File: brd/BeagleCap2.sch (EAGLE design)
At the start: 33 parts, among them IC2 7805TV, J2 DS18B20, J3 Battery, U1 DHT22, X1 Conn BNC : pH, X2 Conn BNC : Dissolved Oxygen, X3 Conn BNC : Conductivity, X4 Conn BNC : ORP

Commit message: Schematic updated with new PCB
Done by JayMcGee
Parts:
- LED1: device led:LED5MM -> led:LEDSML0805
- R1, R10, R2, R3, R4, R5, R6, R7, R8, R9: device adafruit:R-US_0207/10 -> adafruit:R-US_R0805
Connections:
- removed net 3.3V: J2.3, J4.1, R10.1, R2.2, R4.1, R5.2, R6.2, R9.1, U$1.VDD_3V3EXP@2, U$2.VCC, U$3.VCC, U$4.VCC, U$5.VCC, U1.VDD
- new net GNDX: J2.3, R2.2, R4.1, R5.2, R6.2, U$1.VDD_3V3EXP@2, U$2.VCC, U$3.VCC, U$4.VCC, U$5.VCC, U1.VDD
- net 5V: now also J4.1, R10.1, R9.1
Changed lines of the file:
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@@
 <part name="SUPPLY3" library="supply2" deviceset="GND" device=""/>
 <part name="P+2" library="supply1" deviceset="VCC" device="" value="3.3V"/>
-<part name="R1" library="adafruit" deviceset="R-US_" device="0207/10" value="100"/>
-<part name="R2" library="adafruit" deviceset="R-US_" device="0207/10" value="4.7K"/>
-<part name="R3" library="adafruit" deviceset="R-US_" device="0207/10" value="100"/>
-<part name="R4" library="adafruit" deviceset="R-US_" device="0207/10" value="4.7K"/>
+<part name="R1" library="adafruit" deviceset="R-US_" device="R0805" value="100"/>
+<part name="R2" library="adafruit" deviceset="R-US_" device="R0805" value="4.7K"/>
+<part name="R3" library="adafruit" deviceset="R-US_" device="R0805" value="100"/>
+<part name="R4" library="adafruit" deviceset="R-US_" device="R0805" value="4.7K"/>
 <part name="3.3V" library="supply1" deviceset="VCC" device="" value="3.3V"/>
 <part name="IC2" library="linear" deviceset="78*" device="TV" technology="05"/>
@@
 <part name="SUPPLY5" library="supply2" deviceset="GND" device=""/>
 <part name="P+5" library="supply1" deviceset="VCC" device="" value="3.3V"/>
-<part name="R5" library="adafruit" deviceset="R-US_" device="0207/10" value="4.7K"/>
-<part name="R6" library="adafruit" deviceset="R-US_" device="0207/10" value="4.7K"/>
+<part name="R5" library="adafruit" deviceset="R-US_" device="R0805" value="4.7K"/>
+<part name="R6" library="adafruit" deviceset="R-US_" device="R0805" value="4.7K"/>
 <part name="SUPPLY6" library="supply2" deviceset="GND" device=""/>
 <part name="BARREL" library="con-wago-500" deviceset="W237-102" device=""/>
 <part name="D1" library="diode" deviceset="1N4004" device="" value="1N4007"/>
 <part name="D2" library="diode" deviceset="1N4004" device="" value="1N4007"/>
-<part name="LED1" library="led" deviceset="LED" device="5MM"/>
-<part name="R7" library="adafruit" deviceset="R-US_" device="0207/10" value="330"/>
-<part name="R8" library="adafruit" deviceset="R-US_" device="0207/10" value="1K"/>
+<part name="LED1" library="led" deviceset="LED" device="SML0805"/>
+<part name="R7" library="adafruit" deviceset="R-US_" device="R0805" value="330"/>
+<part name="R8" library="adafruit" deviceset="R-US_" device="R0805" value="1K"/>
 <part name="D3" library="diode" deviceset="1N4148" device="DO35-10"/>
-<part name="R9" library="adafruit" deviceset="R-US_" device="0207/10" value="4.7K"/>
+<part name="R9" library="adafruit" deviceset="R-US_" device="R0805" value="4.7K"/>
 <part name="D4" library="diode" deviceset="1N4148" device="DO35-10"/>
-<part name="R10" library="adafruit" deviceset="R-US_" device="0207/10" value="4.7K"/>
-<part name="SUPPLY7" library="supply2" deviceset="VCC" device=""/>
+<part name="R10" library="adafruit" deviceset="R-US_" device="R0805" value="4.7K"/>
 <part name="J2" library="con-amp" deviceset="MTA03-100" device="" value="DS18B20"/>
 <part name="J3" library="con-amp" deviceset="MTA03-100" device="" value="Battery"/>
@@
 <instance part="D4" gate="G$1" x="83.82" y="-49.53"/>
 <instance part="R10" gate="G$1" x="101.6" y="-34.29" rot="R270"/>
-<instance part="SUPPLY7" gate="G$1" x="88.9" y="-24.13"/>
 <instance part="J2" gate="G$1" x="-66.04" y="104.14" rot="R90"/>
 <instance part="J3" gate="G$1" x="-8.89" y="154.94" rot="R90"/>
@@
 </segment>
 </net>
-<net name="3.3V" class="0">
+<net name="GNDX" class="0">
 <segment>
 <wire x1="76.2" y1="45.72" x2="76.2" y2="48.26" width="0.1524" layer="91"/>
@@
 <pinref part="R6" gate="G$1" pin="2"/>
 <wire x1="92.71" y1="41.91" x2="92.71" y2="39.37" width="0.1524" layer="91"/>
-</segment>
-<segment>
-<pinref part="SUPPLY7" gate="G$1" pin="VCC"/>
-<wire x1="88.9" y1="-26.67" x2="88.9" y2="-27.94" width="0.1524" layer="91"/>
-<pinref part="R9" gate="G$1" pin="1"/>
-<wire x1="92.71" y1="-29.21" x2="92.71" y2="-27.94" width="0.1524" layer="91"/>
-<wire x1="92.71" y1="-27.94" x2="88.9" y2="-27.94" width="0.1524" layer="91"/>
-<pinref part="R10" gate="G$1" pin="1"/>
-<wire x1="101.6" y1="-29.21" x2="101.6" y2="-27.94" width="0.1524" layer="91"/>
-<wire x1="101.6" y1="-27.94" x2="92.71" y2="-27.94" width="0.1524" layer="91"/>
-<junction x="92.71" y="-27.94"/>
-<wire x1="101.6" y1="-27.94" x2="106.68" y2="-27.94" width="0.1524" layer="91"/>
-<junction x="101.6" y="-27.94"/>
-<wire x1="106.68" y1="-27.94" x2="106.68" y2="-40.64" width="0.1524" layer="91"/>
-<pinref part="J4" gate="G$1" pin="1"/>
-<wire x1="106.68" y1="-40.64" x2="125.73" y2="-40.64" width="0.1524" layer="91"/>
 </segment>
 </net>
@@
 <wire x1="66.04" y1="156.21" x2="66.04" y2="157.48" width="0.1524" layer="91"/>
 <junction x="66.04" y="157.48"/>
-</segment>
-</net>
+<label x="66.04" y="158.75" size="1.778" layer="95"/>
+</segment>
+<segment>
+<pinref part="R9" gate="G$1" pin="1"/>
+<wire x1="92.71" y1="-29.21" x2="92.71" y2="-27.94" width="0.1524" layer="91"/>
+<wire x1="92.71" y1="-27.94" x2="101.6" y2="-27.94" width="0.1524" layer="91"/>
+<pinref part="R10" gate="G$1" pin="1"/>
+<wire x1="101.6" y1="-27.94" x2="101.6" y2="-29.21" width="0.1524" layer="91"/>
+<wire x1="101.6" y1="-27.94" x2="106.68" y2="-27.94" width="0.1524" layer="91"/>
+<junction x="101.6" y="-27.94"/>
+<wire x1="106.68" y1="-27.94" x2="106.68" y2="-40.64" width="0.1524" layer="91"/>
+<pinref part="J4" gate="G$1" pin="1"/>
+<wire x1="106.68" y1="-40.64" x2="125.73" y2="-40.64" width="0.1524" layer="91"/>
+<label x="92.71" y="-27.94" size="1.778" layer="95"/>
+<wire x1="92.71" y1="-27.94" x2="90.17" y2="-27.94" width="0.1524" layer="91"/>
+<junction x="92.71" y="-27.94"/>
+<wire x1="90.17" y1="-27.94" x2="90.17" y2="-24.13" width="0.1524" layer="91"/>
+</segment>
+</net>

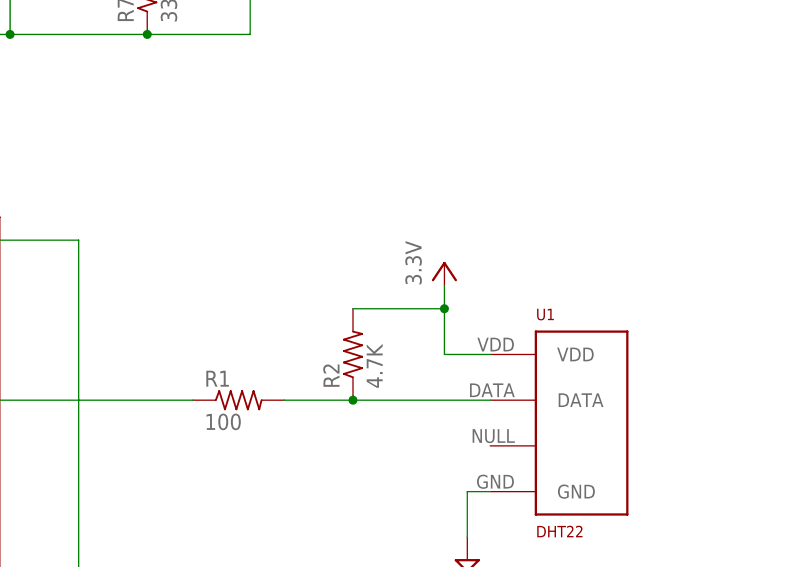
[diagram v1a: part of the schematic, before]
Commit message: Pcb updated, Fixed DRU error
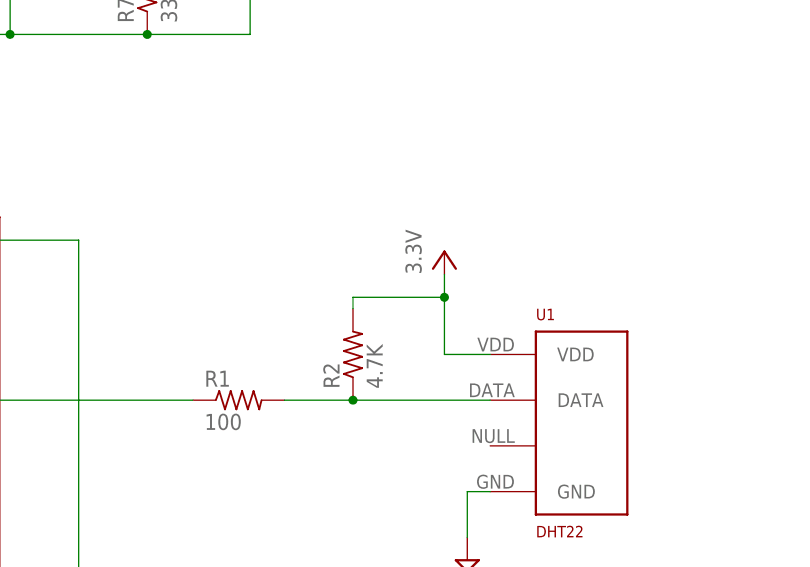
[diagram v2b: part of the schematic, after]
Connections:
- net GNDX renamed 3.3V
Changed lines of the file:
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@@
 <grid distance="0.05" unitdist="inch" unit="inch" style="lines" multiple="1" display="no" altdistance="0.01" altunitdist="inch" altunit="inch"/>
 <layers>
-<layer number="1" name="Top" color="4" fill="1" visible="yes" active="no"/>
-<layer number="2" name="Route2" color="1" fill="3" visible="yes" active="no"/>
-<layer number="3" name="Route3" color="4" fill="3" visible="yes" active="no"/>
-<layer number="4" name="Route4" color="1" fill="4" visible="yes" active="no"/>
-<layer number="5" name="Route5" color="4" fill="4" visible="yes" active="no"/>
-<layer number="6" name="Route6" color="1" fill="8" visible="yes" active="no"/>
-<layer number="7" name="Route7" color="4" fill="8" visible="yes" active="no"/>
-<layer number="8" name="Route8" color="1" fill="2" visible="yes" active="no"/>
-<layer number="9" name="Route9" color="4" fill="2" visible="yes" active="no"/>
-<layer number="10" name="Route10" color="1" fill="7" visible="yes" active="no"/>
-<layer number="11" name="Route11" color="4" fill="7" visible="yes" active="no"/>
-<layer number="12" name="Route12" color="1" fill="5" visible="yes" active="no"/>
-<layer number="13" name="Route13" color="4" fill="5" visible="yes" active="no"/>
-<layer number="14" name="Route14" color="1" fill="6" visible="yes" active="no"/>
-<layer number="15" name="Route15" color="4" fill="6" visible="yes" active="no"/>
-<layer number="16" name="Bottom" color="1" fill="1" visible="yes" active="no"/>
-<layer number="17" name="Pads" color="2" fill="1" visible="yes" active="no"/>
-<layer number="18" name="Vias" color="2" fill="1" visible="yes" active="no"/>
-<layer number="19" name="Unrouted" color="6" fill="1" visible="yes" active="no"/>
-<layer number="20" name="Dimension" color="15" fill="1" visible="yes" active="no"/>
-<layer number="21" name="tPlace" color="7" fill="1" visible="yes" active="no"/>
-<layer number="22" name="bPlace" color="7" fill="1" visible="yes" active="no"/>
-<layer number="23" name="tOrigins" color="15" fill="1" visible="yes" active="no"/>
-<layer number="24" name="bOrigins" color="15" fill="1" visible="yes" active="no"/>
-<layer number="25" name="tNames" color="7" fill="1" visible="yes" active="no"/>
-<layer number="26" name="bNames" color="7" fill="1" visible="yes" active="no"/>
-<layer number="27" name="tValues" color="7" fill="1" visible="yes" active="no"/>
-<layer number="28" name="bValues" color="7" fill="1" visible="yes" active="no"/>
+<layer number="1" name="Top" color="4" fill="1" visible="no" active="no"/>
+<layer number="2" name="Route2" color="1" fill="3" visible="no" active="no"/>
+<layer number="3" name="Route3" color="4" fill="3" visible="no" active="no"/>
+<layer number="4" name="Route4" color="1" fill="4" visible="no" active="no"/>
+<layer number="5" name="Route5" color="4" fill="4" visible="no" active="no"/>
+<layer number="6" name="Route6" color="1" fill="8" visible="no" active="no"/>
+<layer number="7" name="Route7" color="4" fill="8" visible="no" active="no"/>
+<layer number="8" name="Route8" color="1" fill="2" visible="no" active="no"/>
+<layer number="9" name="Route9" color="4" fill="2" visible="no" active="no"/>
+<layer number="10" name="Route10" color="1" fill="7" visible="no" active="no"/>
+<layer number="11" name="Route11" color="4" fill="7" visible="no" active="no"/>
+<layer number="12" name="Route12" color="1" fill="5" visible="no" active="no"/>
+<layer number="13" name="Route13" color="4" fill="5" visible="no" active="no"/>
+<layer number="14" name="Route14" color="1" fill="6" visible="no" active="no"/>
+<layer number="15" name="Route15" color="4" fill="6" visible="no" active="no"/>
+<layer number="16" name="Bottom" color="1" fill="1" visible="no" active="no"/>
+<layer number="17" name="Pads" color="2" fill="1" visible="no" active="no"/>
+<layer number="18" name="Vias" color="2" fill="1" visible="no" active="no"/>
+<layer number="19" name="Unrouted" color="6" fill="1" visible="no" active="no"/>
+<layer number="20" name="Dimension" color="15" fill="1" visible="no" active="no"/>
+<layer number="21" name="tPlace" color="7" fill="1" visible="no" active="no"/>
+<layer number="22" name="bPlace" color="7" fill="1" visible="no" active="no"/>
+<layer number="23" name="tOrigins" color="15" fill="1" visible="no" active="no"/>
+<layer number="24" name="bOrigins" color="15" fill="1" visible="no" active="no"/>
+<layer number="25" name="tNames" color="7" fill="1" visible="no" active="no"/>
+<layer number="26" name="bNames" color="7" fill="1" visible="no" active="no"/>
+<layer number="27" name="tValues" color="7" fill="1" visible="no" active="no"/>
+<layer number="28" name="bValues" color="7" fill="1" visible="no" active="no"/>
 <layer number="29" name="tStop" color="7" fill="3" visible="no" active="no"/>
 <layer number="30" name="bStop" color="7" fill="6" visible="no" active="no"/>
@@
 <layer number="35" name="tGlue" color="7" fill="4" visible="no" active="no"/>
 <layer number="36" name="bGlue" color="7" fill="5" visible="no" active="no"/>
-<layer number="37" name="tTest" color="7" fill="1" visible="yes" active="no"/>
-<layer number="38" name="bTest" color="7" fill="1" visible="yes" active="no"/>
+<layer number="37" name="tTest" color="7" fill="1" visible="no" active="no"/>
+<layer number="38" name="bTest" color="7" fill="1" visible="no" active="no"/>
 <layer number="39" name="tKeepout" color="4" fill="11" visible="no" active="no"/>
 <layer number="40" name="bKeepout" color="1" fill="11" visible="no" active="no"/>
@@
 <layer number="44" name="Drills" color="7" fill="1" visible="no" active="no"/>
 <layer number="45" name="Holes" color="7" fill="1" visible="no" active="no"/>
-<layer number="46" name="Milling" color="3" fill="1" visible="yes" active="no"/>
-<layer number="47" name="Measures" color="7" fill="1" visible="yes" active="no"/>
-<layer number="48" name="Document" color="7" fill="1" visible="yes" active="no"/>
-<layer number="49" name="Reference" color="7" fill="1" visible="yes" active="no"/>
-<layer number="50" name="dxf" color="7" fill="1" visible="yes" active="no"/>
-<layer number="51" name="tDocu" color="7" fill="1" visible="yes" active="no"/>
-<layer number="52" name="bDocu" color="7" fill="1" visible="yes" active="no"/>
-<layer number="53" name="tGND_GNDA" color="7" fill="9" visible="yes" active="no"/>
-<layer number="54" name="bGND_GNDA" color="1" fill="9" visible="yes" active="no"/>
-<layer number="56" name="wert" color="7" fill="1" visible="yes" active="no"/>
-<layer number="57" name="tCAD" color="7" fill="1" visible="yes" active="no"/>
+<layer number="46" name="Milling" color="3" fill="1" visible="no" active="no"/>
+<layer number="47" name="Measures" color="7" fill="1" visible="no" active="no"/>
+<layer number="48" name="Document" color="7" fill="1" visible="no" active="no"/>
+<layer number="49" name="Reference" color="7" fill="1" visible="no" active="no"/>
+<layer number="50" name="dxf" color="7" fill="1" visible="no" active="no"/>
+<layer number="51" name="tDocu" color="7" fill="1" visible="no" active="no"/>
+<layer number="52" name="bDocu" color="7" fill="1" visible="no" active="no"/>
+<layer number="53" name="tGND_GNDA" color="7" fill="9" visible="no" active="no"/>
+<layer number="54" name="bGND_GNDA" color="1" fill="9" visible="no" active="no"/>
+<layer number="56" name="wert" color="7" fill="1" visible="no" active="no"/>
+<layer number="57" name="tCAD" color="7" fill="1" visible="no" active="no"/>
 <layer number="91" name="Nets" color="2" fill="1" visible="yes" active="yes"/>
 <layer number="92" name="Busses" color="1" fill="1" visible="yes" active="yes"/>
@@
 <instance part="U1" gate="G$1" x="114.3" y="93.98"/>
 <instance part="SUPPLY3" gate="GND" x="101.6" y="78.74"/>
-<instance part="P+2" gate="VCC" x="99.06" y="111.76"/>
+<instance part="P+2" gate="VCC" x="99.06" y="113.03"/>
 <instance part="R1" gate="G$1" x="76.2" y="96.52"/>
 <instance part="R2" gate="G$1" x="88.9" y="101.6" rot="R90"/>
@@
 </segment>
 </net>
-<net name="GNDX" class="0">
+<net name="3.3V" class="0">
 <segment>
 <wire x1="76.2" y1="45.72" x2="76.2" y2="48.26" width="0.1524" layer="91"/>
@@
 <wire x1="104.14" y1="101.6" x2="99.06" y2="101.6" width="0.1524" layer="91"/>
 <pinref part="P+2" gate="VCC" pin="VCC"/>
-<wire x1="99.06" y1="101.6" x2="99.06" y2="106.68" width="0.1524" layer="91"/>
+<wire x1="99.06" y1="101.6" x2="99.06" y2="107.95" width="0.1524" layer="91"/>
 <pinref part="R2" gate="G$1" pin="2"/>
-<wire x1="99.06" y1="106.68" x2="99.06" y2="109.22" width="0.1524" layer="91"/>
-<wire x1="88.9" y1="106.68" x2="99.06" y2="106.68" width="0.1524" layer="91"/>
-<junction x="99.06" y="106.68"/>
-</segment>
-<segment>
+<wire x1="99.06" y1="107.95" x2="99.06" y2="110.49" width="0.1524" layer="91"/>
+<wire x1="88.9" y1="106.68" x2="88.9" y2="107.95" width="0.1524" layer="91"/>
+<wire x1="88.9" y1="107.95" x2="99.06" y2="107.95" width="0.1524" layer="91"/>
+<junction x="99.06" y="107.95"/>
+</segment>
+<segment>

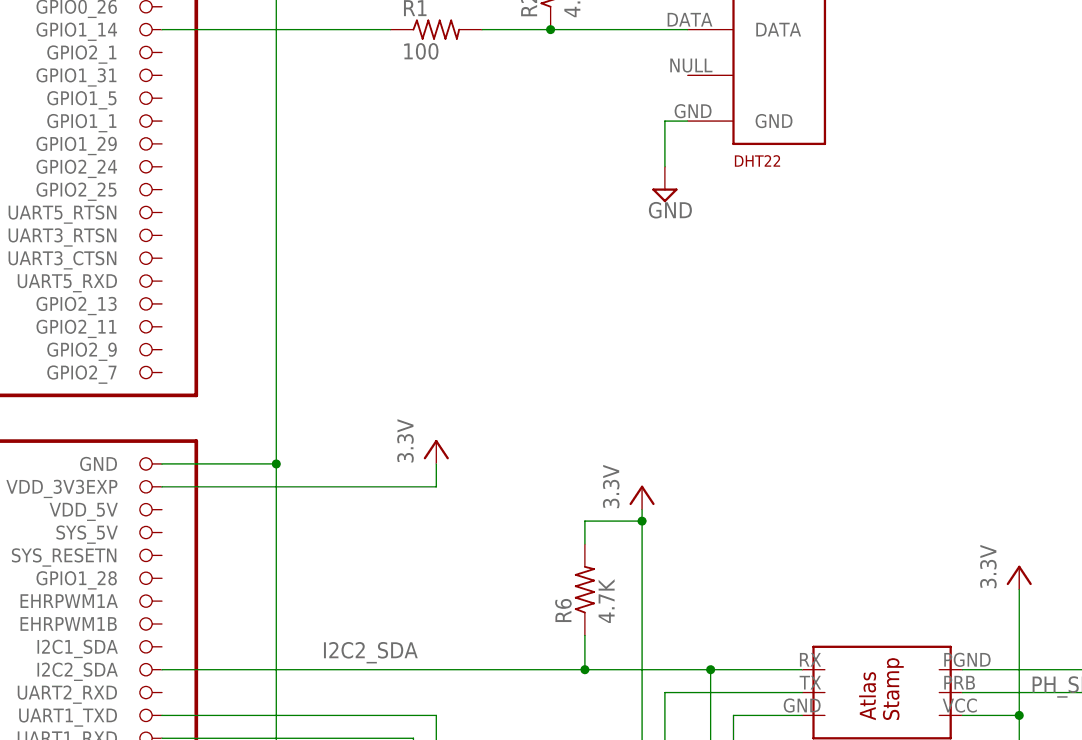
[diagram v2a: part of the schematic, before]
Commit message: Added a switch to select mode of operation
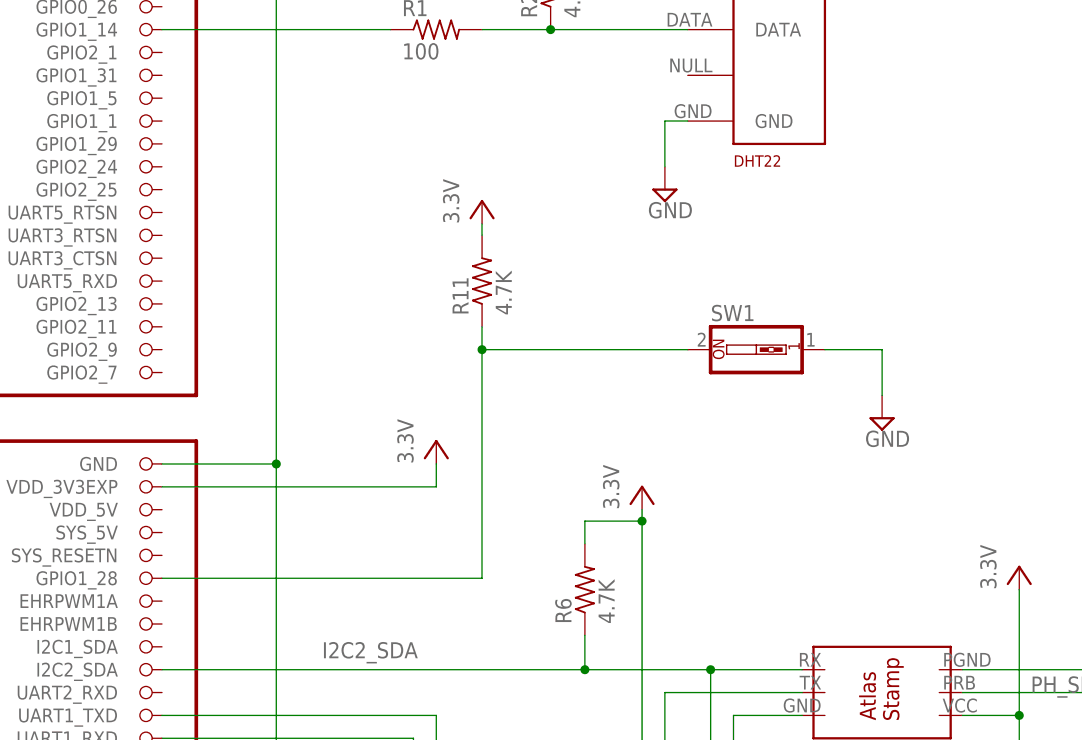
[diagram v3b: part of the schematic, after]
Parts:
- added R11: 4.7K, adafruit:R-US_R0805
- added SW1: (no value), special:SW_DIP-1
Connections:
- new net N$7: R11.1, SW1.2, U$1.GPIO1_28
- new net VCC: R11.2
- net GND: now also SW1.1
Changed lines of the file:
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@@
 <part name="J4" library="con-amp" deviceset="MTA05-100" device=""/>
 <part name="SUPPLY8" library="supply2" deviceset="GND" device=""/>
+<part name="SW1" library="special" deviceset="SW_DIP-1" device=""/>
+<part name="R11" library="adafruit" deviceset="R-US_" device="R0805" value="4.7K"/>
+<part name="P+3" library="supply1" deviceset="VCC" device="" value="3.3V"/>
+<part name="SUPPLY7" library="supply2" deviceset="GND" device=""/>
 </parts>
 <sheets>
@@
 <instance part="J4" gate="G$1" x="128.27" y="-45.72" rot="R270"/>
 <instance part="SUPPLY8" gate="GND" x="124.46" y="-55.88"/>
+<instance part="SW1" gate="G$1" x="111.76" y="60.96"/>
+<instance part="R11" gate="G$1" x="81.28" y="68.58" rot="R90"/>
+<instance part="P+3" gate="VCC" x="81.28" y="77.47"/>
+<instance part="SUPPLY7" gate="GND" x="125.73" y="53.34"/>
 </instances>
 <busses>
@@
 <wire x1="124.46" y1="-50.8" x2="125.73" y2="-50.8" width="0.1524" layer="91"/>
 </segment>
+<segment>
+<pinref part="SW1" gate="G$1" pin="1"/>
+<pinref part="SUPPLY7" gate="GND" pin="GND"/>
+<wire x1="119.38" y1="60.96" x2="125.73" y2="60.96" width="0.1524" layer="91"/>
+<wire x1="125.73" y1="60.96" x2="125.73" y2="55.88" width="0.1524" layer="91"/>
+</segment>
 </net>
 <net name="3.3V" class="0">
@@
 </segment>
 </net>
+<net name="N$7" class="0">
+<segment>
+<pinref part="U$1" gate="G$1" pin="GPIO1_28"/>
+<wire x1="45.72" y1="35.56" x2="81.28" y2="35.56" width="0.1524" layer="91"/>
+<wire x1="81.28" y1="35.56" x2="81.28" y2="60.96" width="0.1524" layer="91"/>
+<pinref part="SW1" gate="G$1" pin="2"/>
+<wire x1="81.28" y1="60.96" x2="104.14" y2="60.96" width="0.1524" layer="91"/>
+<pinref part="R11" gate="G$1" pin="1"/>
+<wire x1="81.28" y1="63.5" x2="81.28" y2="60.96" width="0.1524" layer="91"/>
+<junction x="81.28" y="60.96"/>
+</segment>
+</net>
+<net name="VCC" class="0">
+<segment>
+<pinref part="P+3" gate="VCC" pin="VCC"/>
+<pinref part="R11" gate="G$1" pin="2"/>
+<wire x1="81.28" y1="74.93" x2="81.28" y2="73.66" width="0.1524" layer="91"/>
+</segment>
+</net>
